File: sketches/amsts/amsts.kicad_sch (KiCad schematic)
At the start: 10 parts

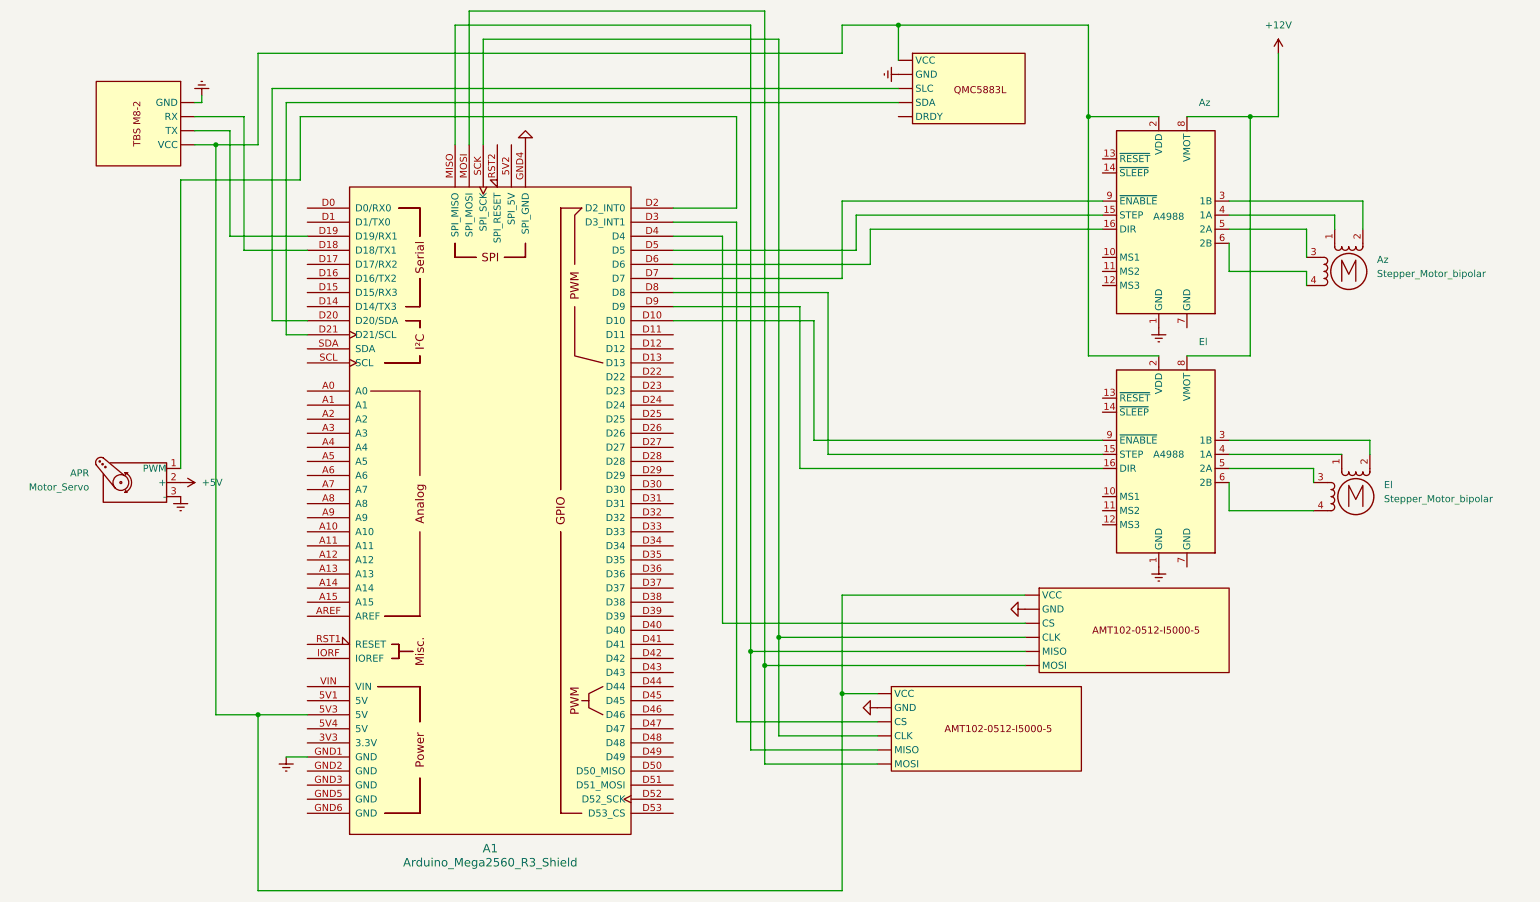
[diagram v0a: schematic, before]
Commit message: Update hardware models and add raw STEP exports
Updated several Inventor part and assembly files in the hardware directory. Added new raw STEP and IPT files for 4x2020, Connect_u2020, H-Connector_2020, and manual locker components. Updated versioned backups in OldVersions. Also updated BOM spreadsheet and electronics schematic and PDF, with minor changes to encoder and main Arduino code.
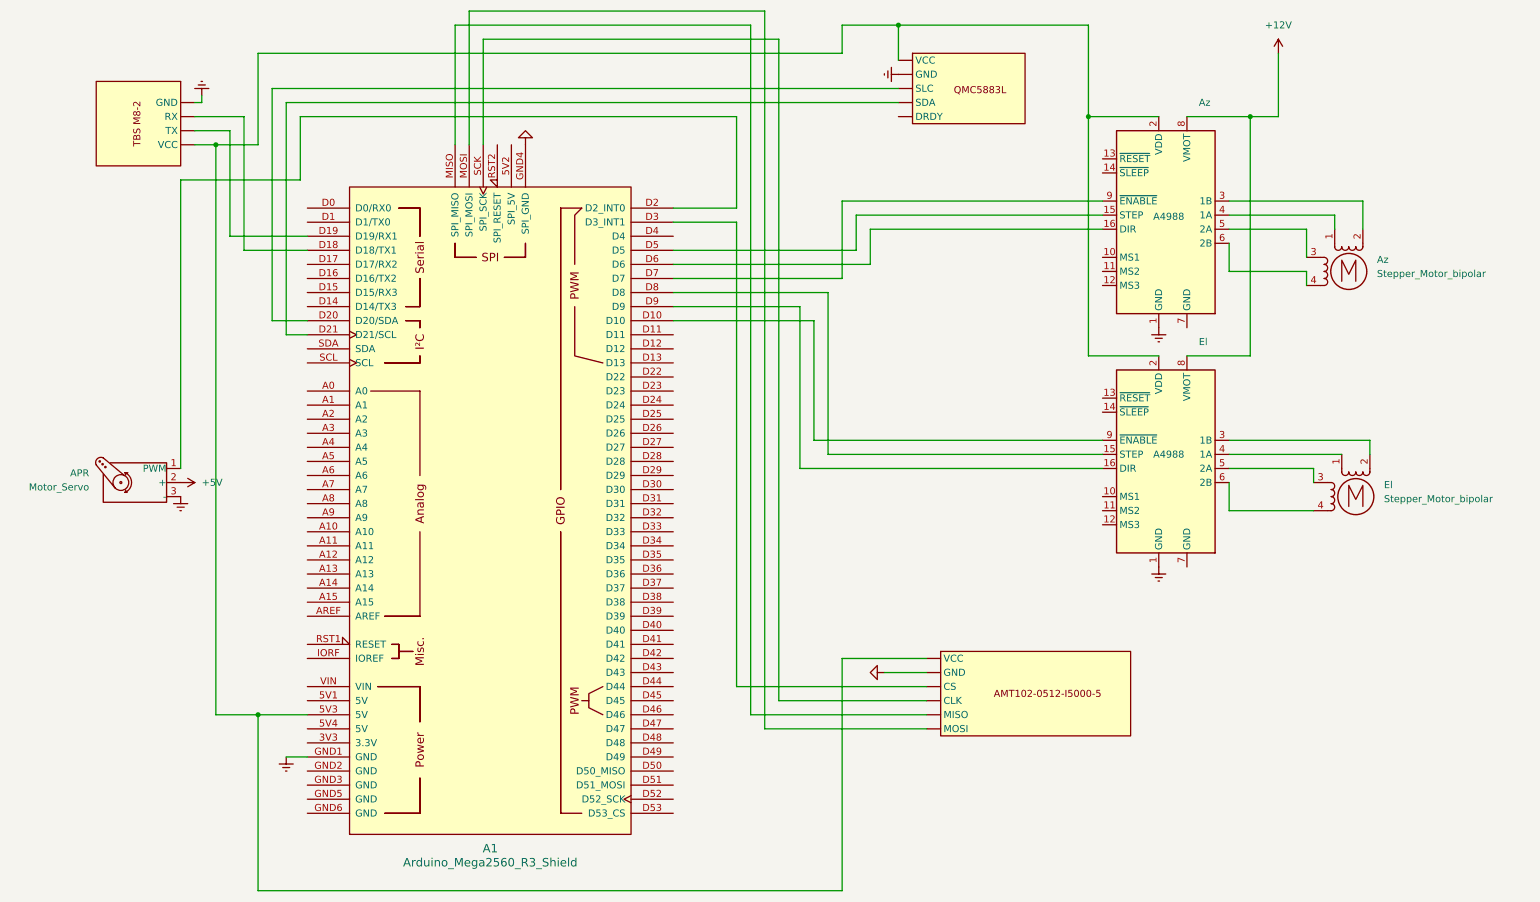
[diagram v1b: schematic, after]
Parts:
- removed U3: ~, symbol my_symbols:AMT22
